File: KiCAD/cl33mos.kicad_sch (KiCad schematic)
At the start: 13 parts, among them J1 Edge2x6_Connector, J2 USB_B_Micro, U1 ESP32-WROOM-32, U2 AMS1117-3.3

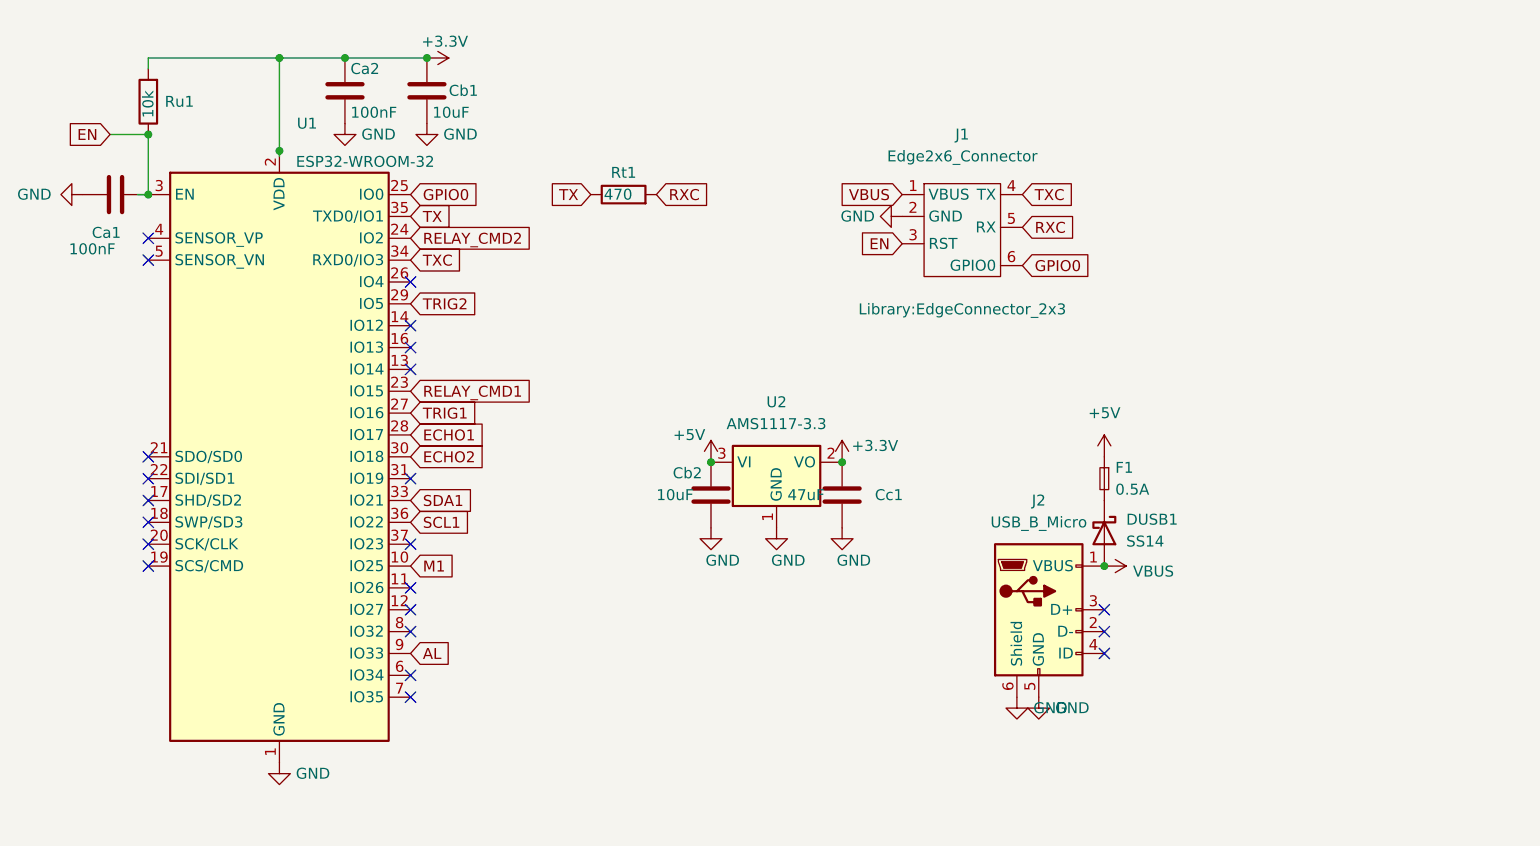
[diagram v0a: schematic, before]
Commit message: four-sonar board (#25)
The four-sonar board written about in [Dual Sonar ESP32 Garage State
Estimation](https://selectiveappeal.org/posts/garage133-dual-sonar/).

- Board supports front and back sonars for both right and left garage
bays.
- Software update for dual-observation hmm, training update.
  - Distinct states for door open with car present and not present.
- Updated ebox design, sencil fixture
- Updated device web interface
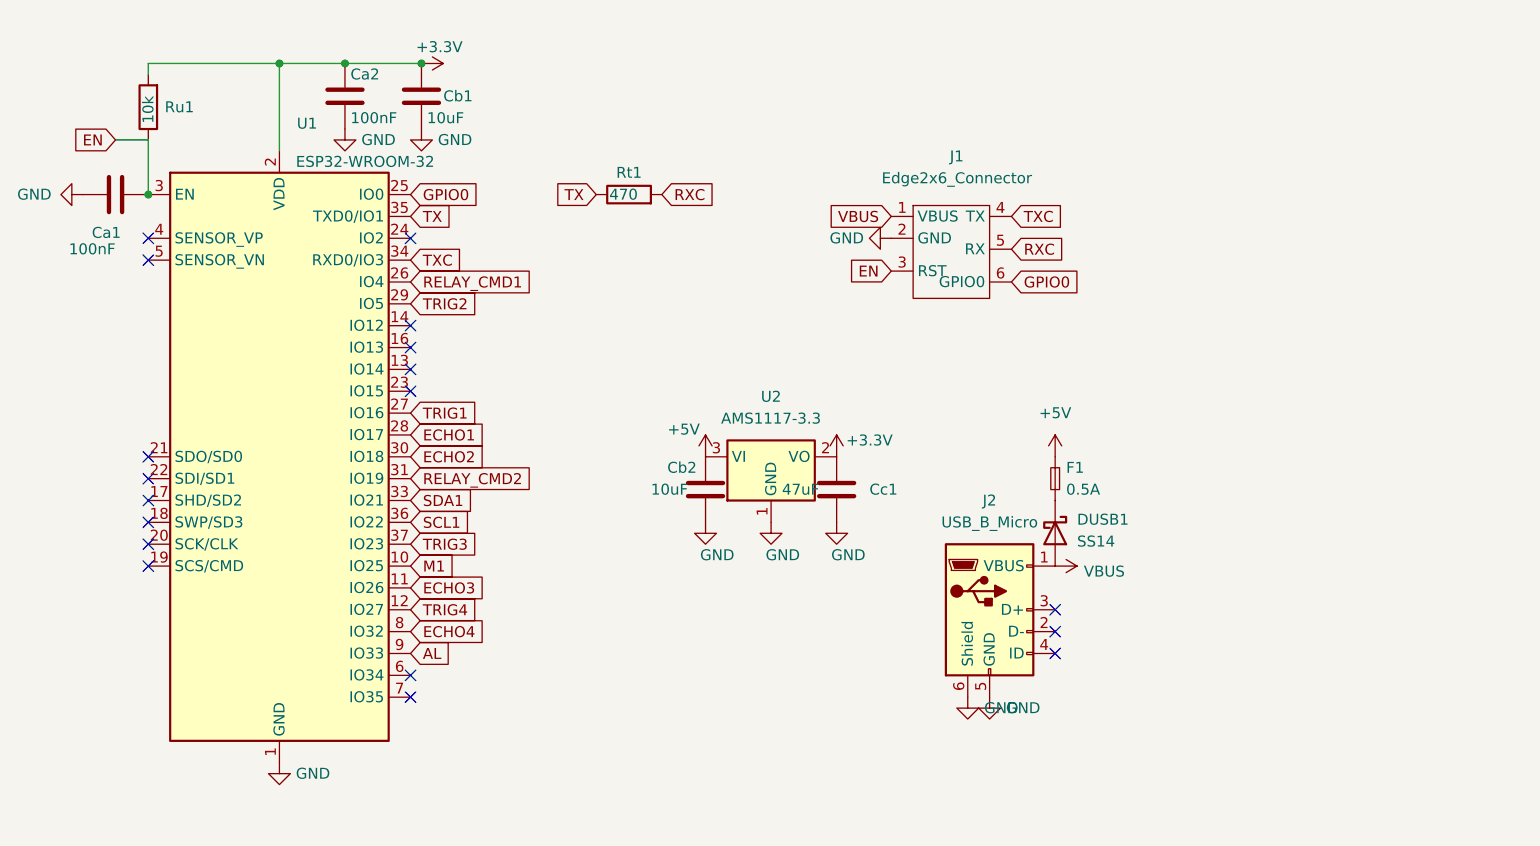
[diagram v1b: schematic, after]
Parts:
- J1: footprint Library:EdgeConnector_2x3 -> chl33_library:EdgeConnector_2x3
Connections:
- net RELAY_CMD1: now also U1.26 (IO4); no longer U1.23 (IO15)
- net RELAY_CMD2: now also U1.31 (IO19); no longer U1.24 (IO2)
- net ECHO3: now reaches U1.11 (IO26)
- net TRIG4: now reaches U1.12 (IO27)
- net TRIG3: now reaches U1.37 (IO23)
- net ECHO4: now reaches U1.8 (IO32)
- no-connect marks 22 -> 18
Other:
- moved on the sheet: Ca2, Cb1, Cb2, Cc1, DUSB1, F1, J1, J2, Rt1, Ru1, U2

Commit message: Version 2.1.0: four sonars, USB-C (#26)
## [2.1.0] - 2026-10-14

### Added
- **Hardware Board v3.1 & Enclosure Updates**: KiCAD PCB updates for
board v3.1 with revised BOM, updated 3D printable enclosure (better
SHTC3 thermal isolation, labeled connectors, improved USB-C port
clearance), and solder stencil support frame model.
- **HMM Visualization & Retraining Workflow**: Added
`analysis/hmm_to_svg.py` to generate SVG state transition diagrams from
trained HMM models, and added characterization workflow in
`analysis/retrain.py`.

### Changed
- **Sonar Watchdog & Timeout Stability**: Added sonar ping timeout
handling to prevent blocking pulses from triggering the ESP32 hardware
watchdog.

### Removed
- **Retired Legacy Hardware**: Removed firmware and PlatformIO
configuration support for legacy Classic ESP32 boards (Board v1/v2 /
`node32s`), focusing entirely on Board v3.x (ESP32-S3).

## [2.0.0] - 2026-08-21

### Added
- **Hardware Board v3.0 & ESP32-S3 Support**: Added PlatformIO
configuration (`usb_s3`), pin assignments for ESP32-S3, updated
schematic/PCB designs, and refreshed solder stencil fixture 3D models.
- **Quad-Sonar Support**: Integrated dual ultrasonic sensors per side (4
total) with updated state classification logic, training pipeline, and
retrained HMM models.
- **Home Assistant Probability Export**: Exported garage state
probabilities (`probOpen`, `probCar`, `probEmpty`) via Home Assistant
MQTT discovery.

### Changed
- **Svelte Build Tooling**: Pinned `svelteesp32` to v3.2.5 and updated
CI workflows to Node 22 for reproducible builds.
- **Dependency & Workflow Upgrades**: Upgraded `og3` to v0.6.3,
`og3x-oled` to v0.6.1, and updated GitHub Actions workflows to latest
versions.
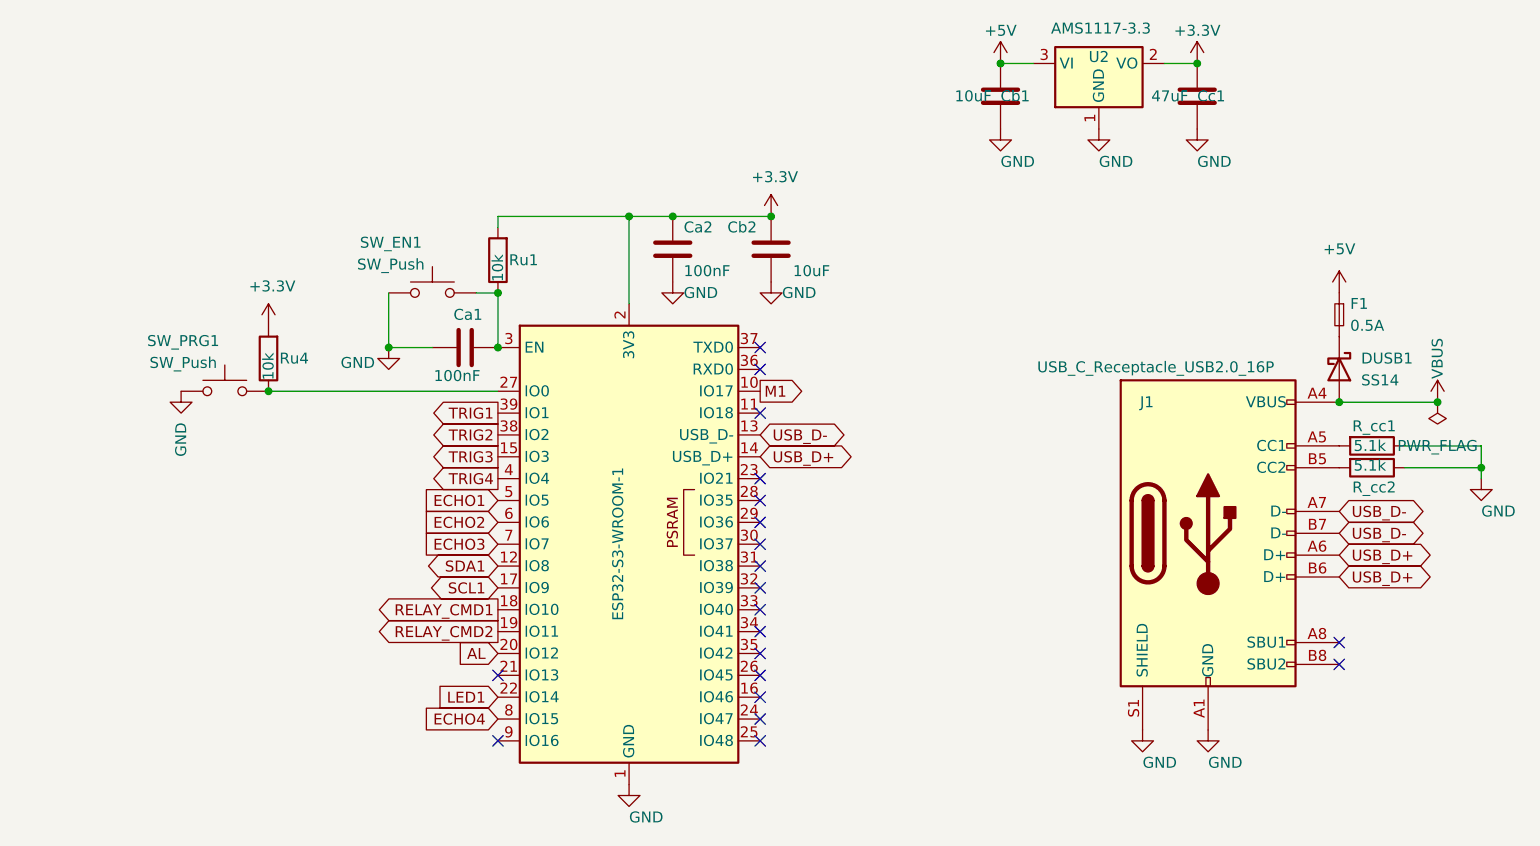
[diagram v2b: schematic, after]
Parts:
- removed J1: Edge2x6_Connector, chl33_library:EdgeConnector_2x3, symbol chl33:Edge2x6_Connector
- removed J2: USB_B_Micro, Connector_USB:USB_Micro-B_Amphenol_10118194_Horizontal, symbol Connector:USB_B_Micro
- removed Rt1: 470, Resistor_SMD:R_0603_1608Metric, symbol Device:R
- removed U1: ESP32-WROOM-32, RF_Module:ESP32-WROOM-32, symbol RF_Module:ESP32-WROOM-32
- added J1: USB_C_Receptacle_USB2.0_16P, Connector_USB:USB_C_Receptacle_HRO_TYPE-C-31-M-12, symbol Connector:USB_C_Receptacle_USB2.0_16P
- added R_cc1, R_cc2: 5.1k, Resistor_SMD:R_0603_1608Metric, symbol Device:R
- added Ru4: 10k, Resistor_SMD:R_0603_1608Metric, symbol Device:R
- added SW_EN1, SW_PRG1: SW_Push, Button_Switch_SMD:SW_SPST_FSMSM, symbol Switch:SW_Push
- added U1: ESP32-S3-WROOM-1, RF_Module:ESP32-S3-WROOM-1, symbol RF_Module:ESP32-S3-WROOM-1
- DUSB1: footprint Diode_SMD:D_2010_5025Metric -> Diode_SMD:D_SMA
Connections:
- net +3.3V: now also Cb2.1, Ru4.2, U1.2 (3V3); no longer Cb1.1
- net +5V: now also Cb1.1; no longer Cb2.1
- net AL: now also U1.20 (IO12)
- net ECHO1: now also U1.5 (IO5)
- net ECHO2: now also U1.6 (IO6)
- net ECHO3: now also U1.7 (IO7)
- net ECHO4: now also U1.8 (IO15)
- net GND: now also J1.A1 (GND), J1.A12 (GND), J1.B1 (GND), J1.B12 (GND), J1.S1 (SHIELD), R_cc1.1, R_cc2.1, SW_EN1.1, SW_PRG1.1, U1.1 (GND), U1.40 (GND), U1.41 (GND)
- net M1: now also U1.10 (IO17)
- net RELAY_CMD1: now also U1.18 (IO10)
- net RELAY_CMD2: now also U1.19 (IO11)
- net SCL1: now also U1.17 (IO9)
- net SDA1: now also U1.12 (IO8)
- net TRIG1: now also U1.39 (IO1)
- net TRIG2: now also U1.38 (IO2)
- net TRIG3: now also U1.15 (IO3)
- net TRIG4: now also U1.4 (IO4)
- net VBUS: now also J1.A4 (VBUS), J1.A9 (VBUS), J1.B4 (VBUS), J1.B9 (VBUS)
- net EN: no longer names the net of Ca1.2, Ru1.1
- net EN: now also SW_EN1.2, U1.3 (EN)
- new net: Ru4.1, SW_PRG1.2, U1.27 (IO0)
- new net: J1.A5 (CC1), R_cc1.2
- new net: J1.B5 (CC2), R_cc2.2
- new net LED1: U1.22 (IO14)
- new net USB_D+: J1.A6 (D+), J1.B6 (D+), U1.14 (USB_D+)
- new net USB_D-: J1.A7 (D-), J1.B7 (D-), U1.13 (USB_D-)
- no-connect marks 18 -> 20
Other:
- moved on the sheet: Ca1, Ca2, Cb1, Cb2, Cc1, DUSB1, F1, Ru1, U2
